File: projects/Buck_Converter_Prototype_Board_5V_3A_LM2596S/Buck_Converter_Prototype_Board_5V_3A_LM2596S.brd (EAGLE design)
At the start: 44.5 x 20.9 mm, 26 parts, among them IC1 TM4C123GH6PM, Q1 NX5032GA

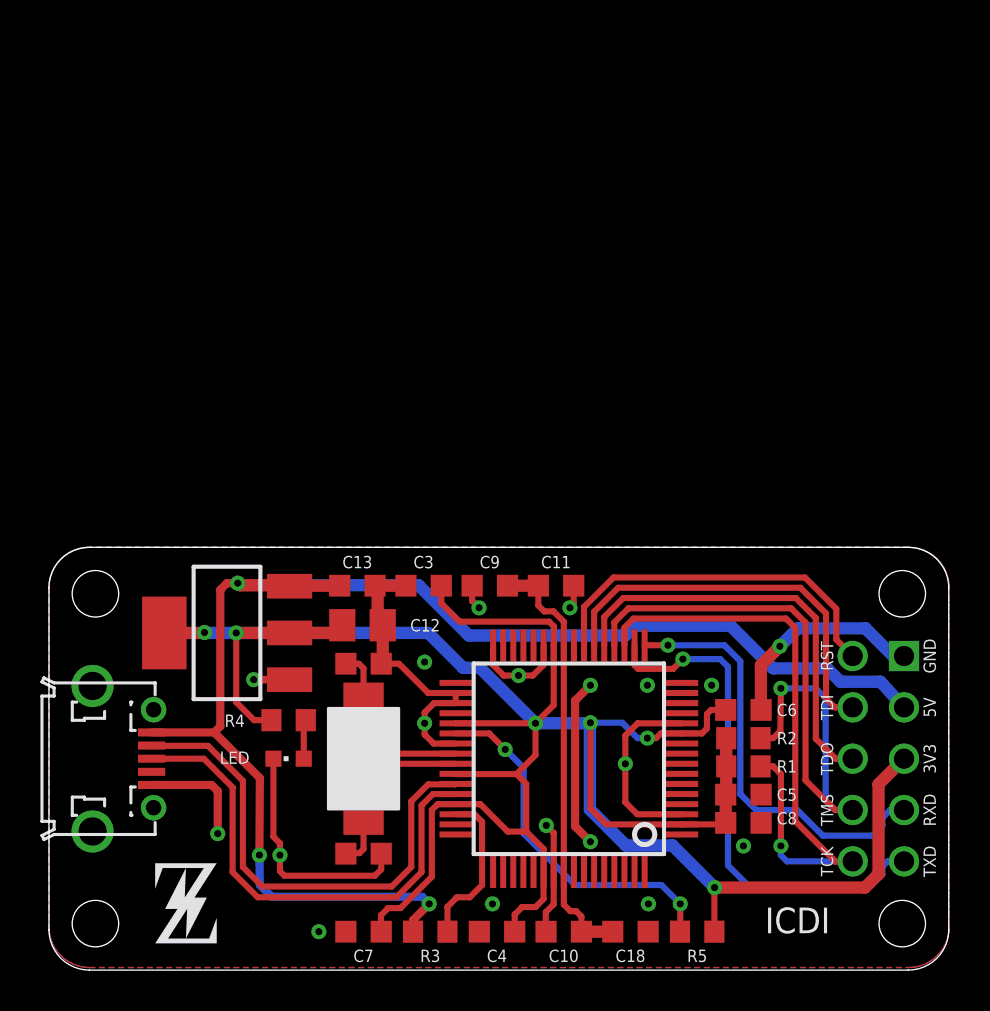
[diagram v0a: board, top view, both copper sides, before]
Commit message: fix some naming and upload UTX EE445M sensor board
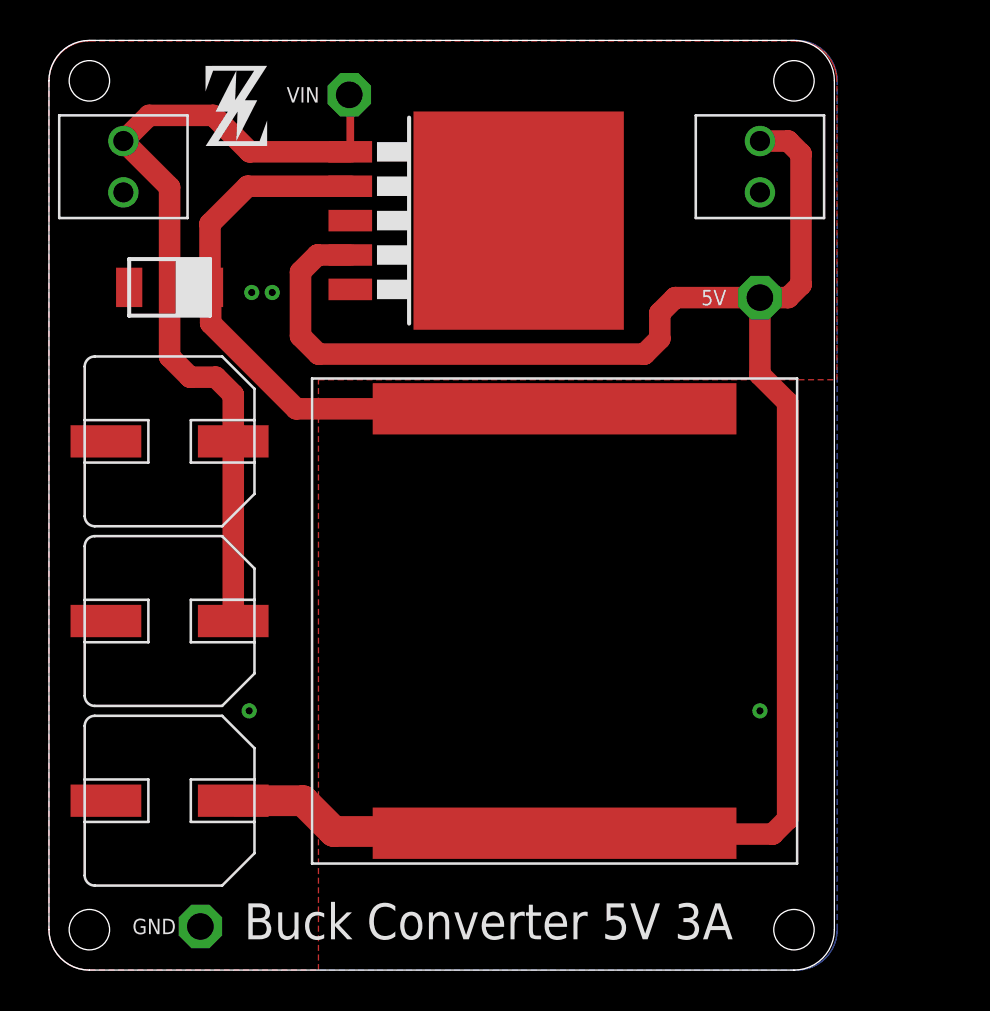
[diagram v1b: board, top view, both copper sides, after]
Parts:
- removed C10, C6, C9: 0.1uF, UT_ECE:C0603K
- removed C11, C7: 1uF, UT_ECE:C0603K
- removed C12: (no value), UT_ECE:C0805K
- removed C13: (no value), UT_ECE:C0603K
- removed C18: 2.2uF, UT_ECE:C0603K
- removed C3, C5, C8: 0.01uF, UT_ECE:C0603K
- removed LED: (no value), adafruit:CHIPLED_0603
- removed Q1: NX5032GA, UT_ECE:NX5032GA
- removed R1, R2, R4, R5: 10k, UT_ECE:R0603
- removed R3: 330, UT_ECE:R0603
- removed U$3: (no value), Z:__LOGO_Z
- removed U$4: _VOLTAGE_REGULATOR_AMS1117, Z:_PACKAGE_SOT223
- added 5V, GND, VIN: TPPAD1-13, testpad:P1-13
- added U$22: POWER_CONNECTOR, Z:_TERMINAL_BLOCK_2.54_1X2
- added U$23: _INDUCTOR_PE-54040SNL, Z:_PACKAGE_HCI-68
- added U$24: _DIODE_SOD128, Z:_PACKAGE_SOD128
- C1, C2: value 10pF -> 330uF, 35V; device UT_ECE:C0603K -> Z:_CAPACITOR_CHEMI-CON_A_HA0_SMD
- C4: value 0.1uF -> 330uF, 35V; device UT_ECE:C0603K -> Z:_CAPACITOR_CHEMI-CON_A_HA0_SMD
- IC1: value TM4C123GH6PM -> (none); device UT_ECE:SQFP-S-10X10-64 -> Z:_PACKAGE_TO263-5
- U$1: value USB_MICRO_PTH -> POWER_CONNECTOR; device Z:USB_MICRO_PTH -> Z:_TERMINAL_BLOCK_2.54_1X2
- U$2: value JTAG_SERIAL -> (none); device Z:JTAG_SERIAL_PTH -> Z:__LOGO_Z
- moved U$1 45.6 mm to (35.2, 39.8), turned to 90 degrees
- moved U$2 45.0 mm to (7.75, 40.8), turned to 0 degrees
- moved IC1 27.1 mm to (20.7, 37.1), turned to 270 degrees
- moved C4 17.4 mm to (5.97, 8.38)
- moved C2 15.0 mm to (5.97, 17.3), turned to 180 degrees
- moved C1 14.6 mm to (5.97, 26.2), turned to 180 degrees
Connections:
- removed net 3V3: C12.1, C3.1, C4.1, C5.1, C6.1, C7.1, C8.1, IC1.11, IC1.2, IC1.26, IC1.37, IC1.42, IC1.45, IC1.54, R1.2, R2.2, R4.2, R5.2, U$2.3V3, U$4.2, U$4.4
- removed net LDO: C10.1, C11.1, C18.1, C9.1, IC1.25, IC1.56
- removed net N$1: LED.A, R4.1
- removed net N$2: IC1.46, R3.1
- removed net N$4: IC1.38, R5.1
- removed net OSC0: C1.1, IC1.40, Q1.1
- removed net OSC1: C2.1, IC1.41, Q1.2
- removed net RST: IC1.23, U$2.RST
- removed net TCK: IC1.19, R1.1, U$2.TCK
- removed net TDI: IC1.22, U$2.TDI
- removed net TDO: IC1.21, U$2.TDO
- removed net TMS: IC1.20, R2.1, U$2.TMS
- removed net UART0_RX: IC1.17, U$2.RXD
- removed net UART0_TX: IC1.18, U$2.TXD
- removed net USB_DM: IC1.43, U$1.2
- removed net USB_DP: IC1.44, U$1.3
- new net N$11: IC1.2, U$23.1, U$24.C
- new net VIN: C1.+, C2.+, IC1.1, U$22.1, VIN.TP
- net 5V: now also 5V.TP, C4.+, IC1.4, U$1.2, U$23.2; no longer C13.1, R3.2, U$1.1, U$2.5V, U$4.3
- net GND: now also C1.-, C2.-, C4.-, GND.TP, IC1.5, IC1.6, U$1.1, U$22.2, U$24.A; no longer C1.2, C10.2, C11.2, C12.2, C13.2, C18.2, C2.2, C3.2, C4.2, C5.2, C6.2, C7.2, C8.2, C9.2, IC1.12, IC1.27, IC1.32, IC1.34, IC1.35, IC1.39, IC1.55, LED.C, U$1.5, U$2.GND, U$4.1
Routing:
- net 3V3: track 130.3 -> 0.00 mm, vias 6 -> 0
- net GND: track 75.1 -> 0.00 mm, vias 19 -> 4
- net VIN: track 0.00 -> 42.1 mm
- net TMS: track 34.2 -> 0.00 mm, vias 1 -> 0
- net TCK: track 31.8 -> 0.00 mm, vias 1 -> 0
- net N$11: track 0.00 -> 31.4 mm
- net UART0_TX: track 25.7 -> 0.00 mm, vias 1 -> 0
- net 5V: track 71.3 -> 96.9 mm, vias 3 -> 0
- net USB_DM: track 24.4 -> 0.00 mm
- net USB_DP: track 24.4 -> 0.00 mm
- net LDO: track 21.5 -> 0.00 mm
- net UART0_RX: track 21.3 -> 0.00 mm, vias 1 -> 0
- net TDO: track 20.9 -> 0.00 mm
- net TDI: track 19.9 -> 0.00 mm
- net RST: track 18.3 -> 0.00 mm
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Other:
- board size 44.5 x 20.9 mm -> 38.9 x 46 mm
- board text added: "Buck Converter 5V 3A"
- board text removed: "ICDI"
